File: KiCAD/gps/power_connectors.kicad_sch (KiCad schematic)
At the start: 36 parts, among them J7 PJ-037A, J8 1758050, J9 CU01SAH0S00, Q1 SQJ746ELP-T1_GE3, Q2 SQJ746ELP-T1_GE3, U1 AP74502QTA8-7, U2 AP22654WU-7, U3 AP74502QTA8-7

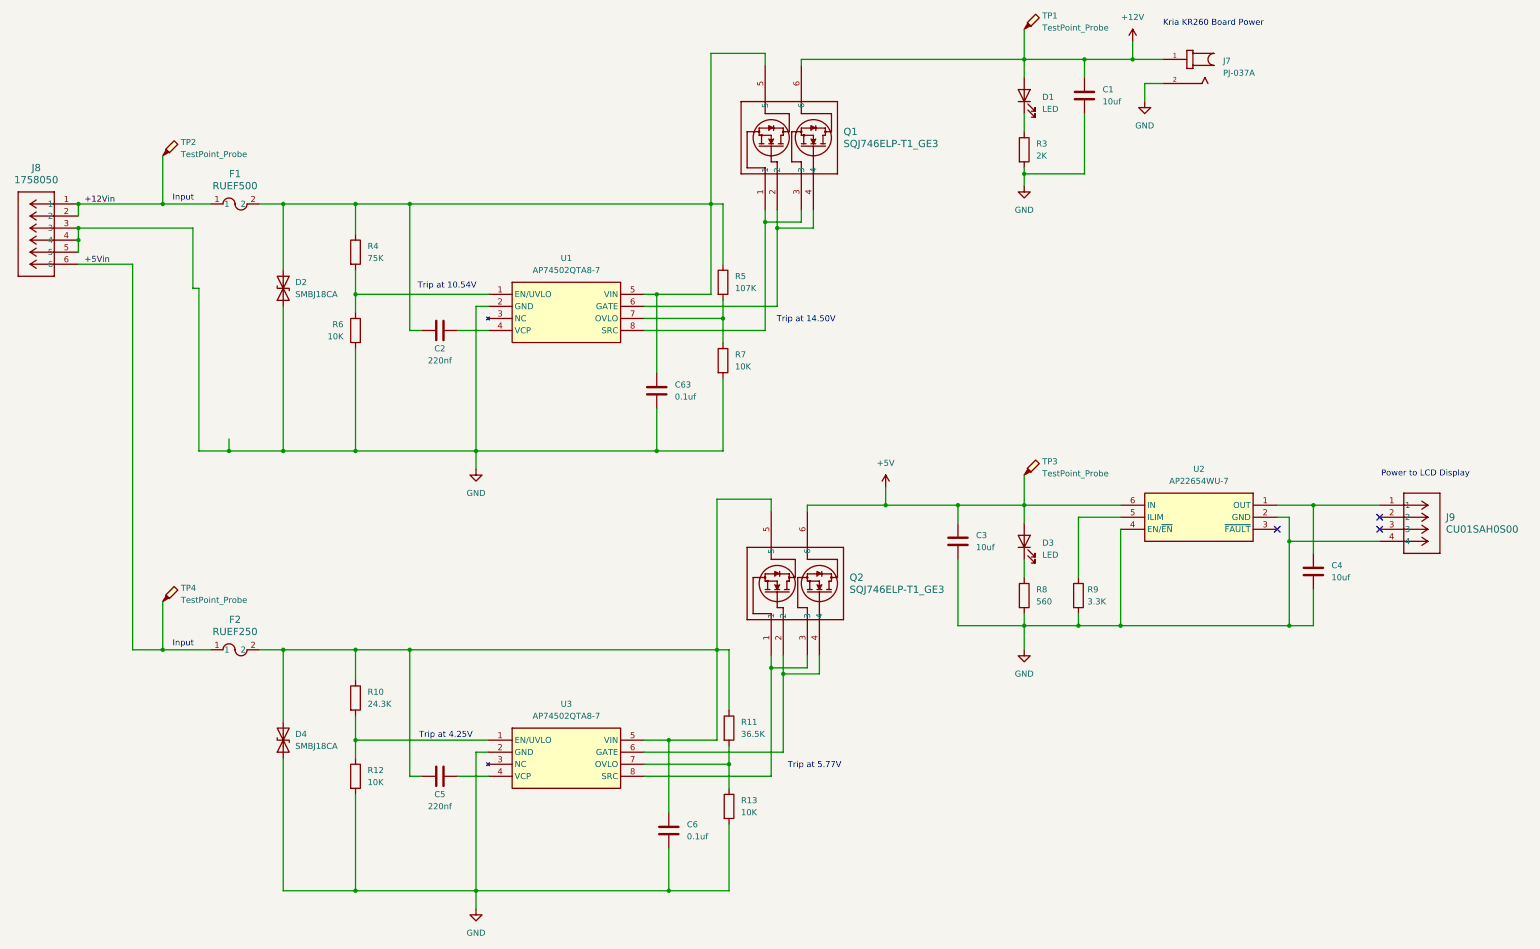
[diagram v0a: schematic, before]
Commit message: Added FPGA debug header and debug LEDs
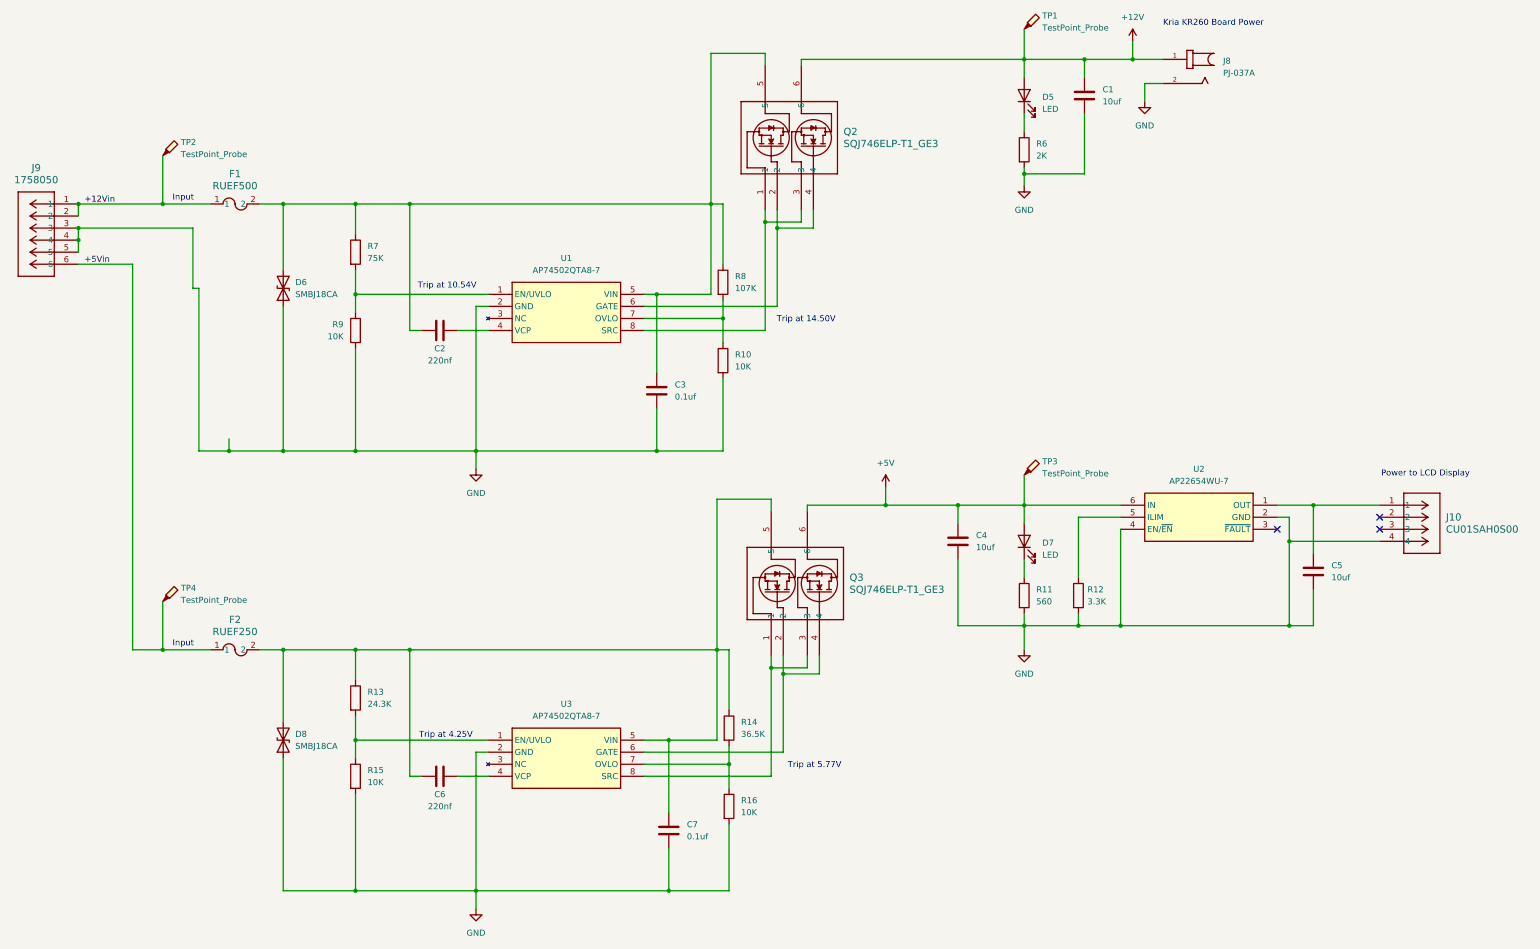
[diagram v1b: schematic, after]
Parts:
- renumbered C63 to C3, C3 to C4, C4 to C5, C5 to C6, C6 to C7, D1 to D5, D2 to D6, D3 to D7, D4 to D8, J9 to J10, J7 to J8, J8 to J9, Q1 to Q2, Q2 to Q3, R7 to R10, R8 to R11, R9 to R12, R10 to R13, R11 to R14, R12 to R15, R13 to R16, R3 to R6, R4 to R7, R5 to R8, R6 to R9
